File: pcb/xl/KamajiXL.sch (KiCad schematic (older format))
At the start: 31 parts

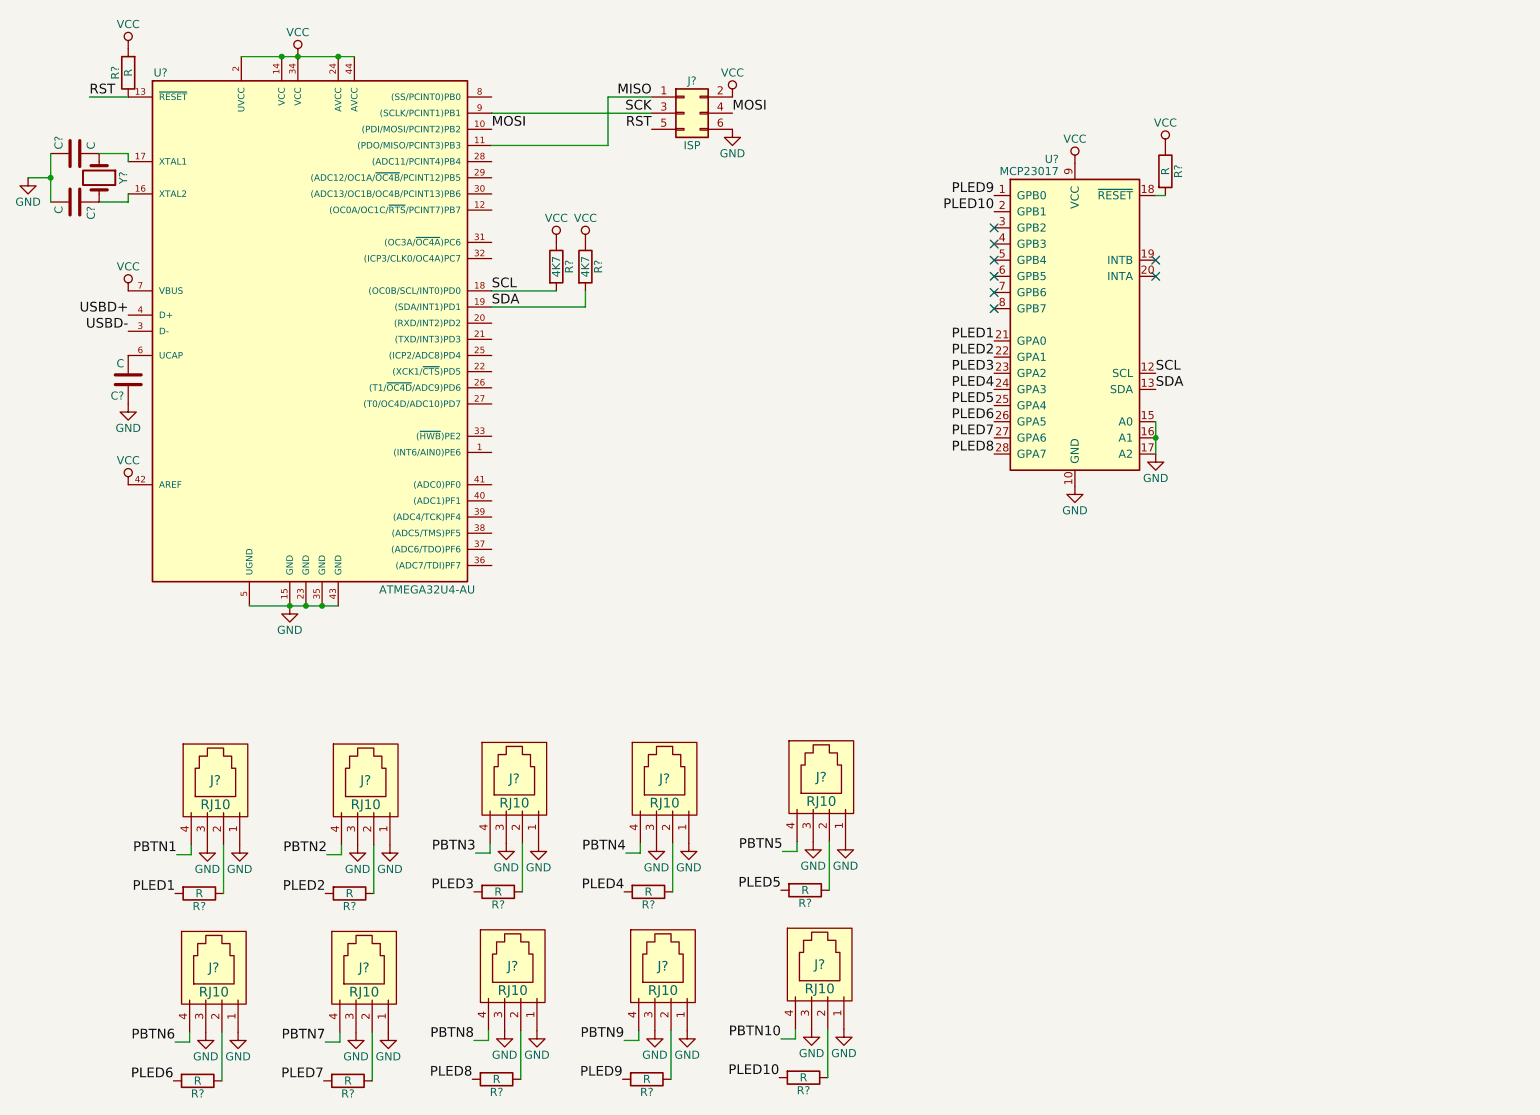
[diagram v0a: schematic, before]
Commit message: put together a minimal schematic for kamaji xl to get an idea about its size
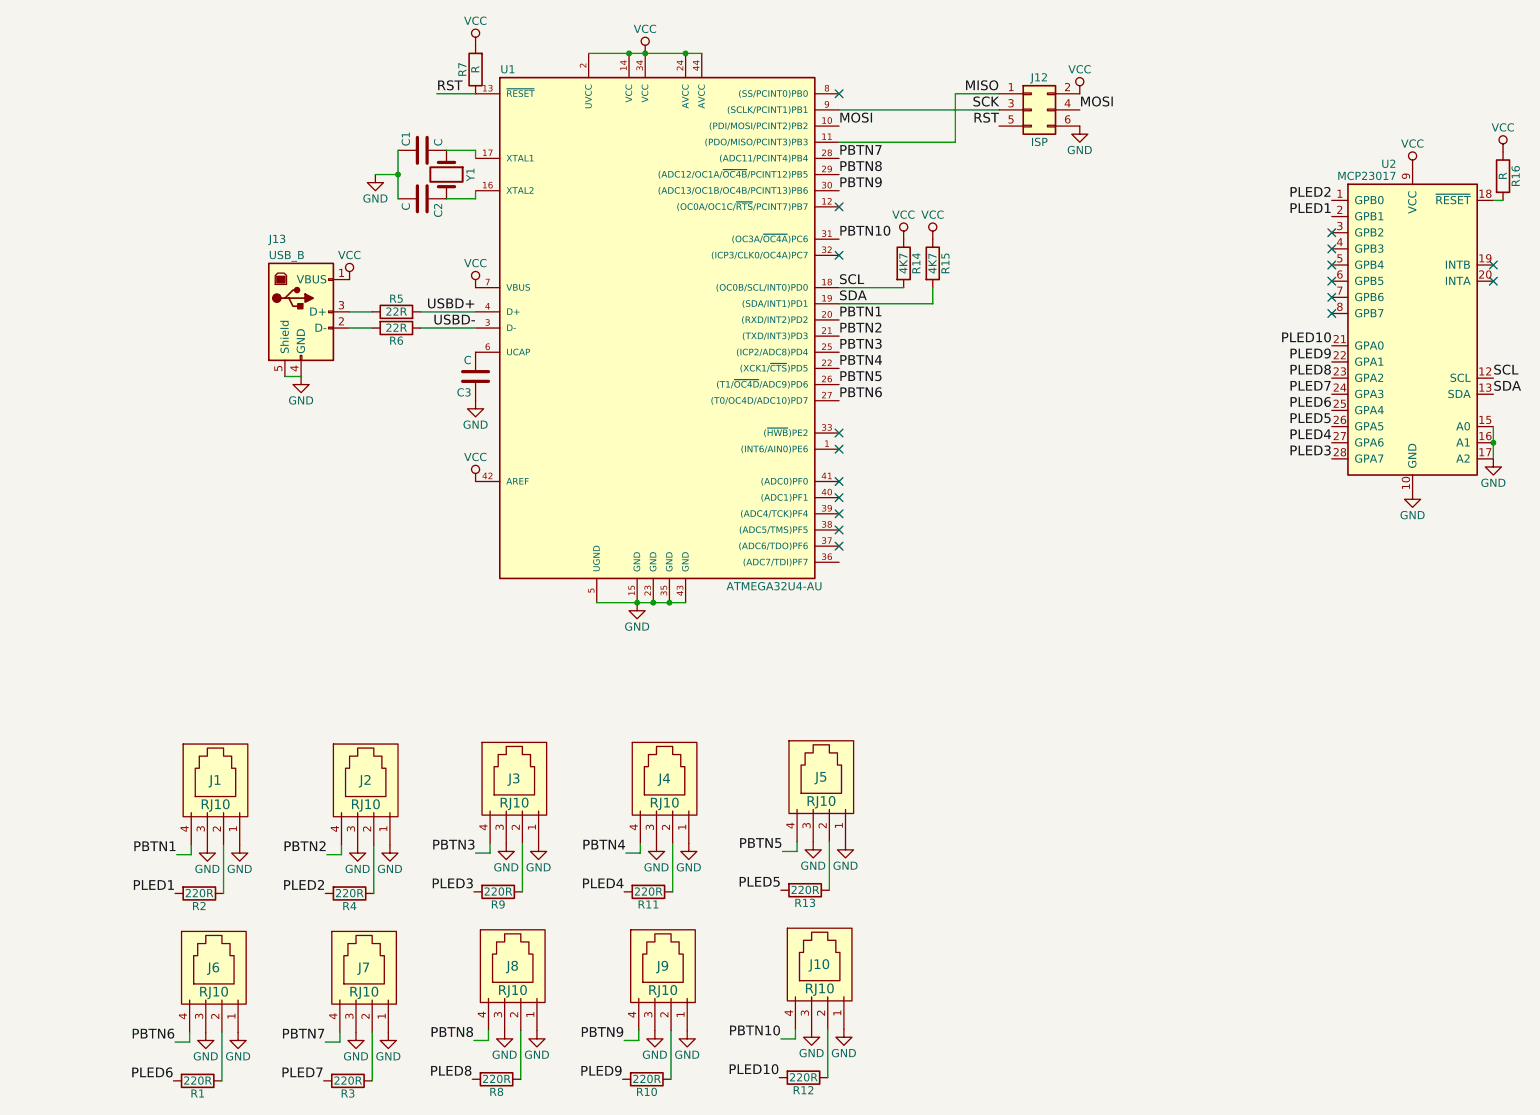
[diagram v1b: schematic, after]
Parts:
- added J13: USB_B, Connectors:USB_B, symbol USB_B
- added R5, R6: 22R, Resistors_SMD:R_1206_HandSoldering, symbol R
- C1, C2, C3: renamed from C?; footprint (none) -> Capacitors_SMD:C_1206_HandSoldering
- J1, J10, J2, J3, J4, J5, J6, J7, J8, J9: renamed from J?; footprint (none) -> kamaji:RJ10
- J12: renamed from J?; footprint (none) -> kamaji:ATmega_ISP_6pin
- R1, R10, R11, R12, R13, R2, R3, R4, R8, R9: renamed from R?; value R -> 220R; footprint (none) -> Resistors_SMD:R_1206_HandSoldering
- R14, R15, R16, R7: renamed from R?; footprint (none) -> Resistors_SMD:R_1206_HandSoldering
- U1: renamed from U?; footprint TQFP44 -> Housings_QFP:TQFP-44_10x10mm_Pitch0.8mm
- U2: renamed from U?; footprint (none) -> Housings_SOIC:SOIC-28W_7.5x17.9mm_Pitch1.27mm
- Y1: renamed from Y?; footprint (none) -> Crystals:Crystal_SMD_HC49-SD_HandSoldering
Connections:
- net GND: now also J13.4 (GND), J13.5 (Shield)
- net PBTN1: now also U1.20 ((RXD/INT2)PD2)
- net PBTN10: now also U1.31 ((OC3A/~OC4A~)PC6)
- net PBTN2: now also U1.21 ((TXD/INT3)PD3)
- net PBTN3: now also U1.25 ((ICP2/ADC8)PD4)
- net PBTN4: now also U1.22 ((XCK1/~CTS~)PD5)
- net PBTN5: now also U1.26 ((T1/~OC4D~/ADC9)PD6)
- net PBTN6: now also U1.27 ((T0/OC4D/ADC10)PD7)
- net PBTN7: now also U1.28 ((ADC11/PCINT4)PB4)
- net PBTN8: now also U1.29 ((ADC12/OC1A/~OC4B~/PCINT12)PB5)
- net PBTN9: now also U1.30 ((ADC13/OC1B/OC4B/PCINT13)PB6)
- net PLED1: now also U2.2 (GPB1); no longer U2.21 (GPA0)
- net PLED10: now also U2.21 (GPA0); no longer U2.2 (GPB1)
- net PLED2: now also U2.1 (GPB0); no longer U2.22 (GPA1)
- net PLED3: now also U2.28 (GPA7); no longer U2.23 (GPA2)
- net PLED4: now also U2.27 (GPA6); no longer U2.24 (GPA3)
- net PLED5: now also U2.26 (GPA5); no longer U2.25 (GPA4)
- net PLED6: now also U2.25 (GPA4); no longer U2.26 (GPA5)
- net PLED7: now also U2.24 (GPA3); no longer U2.27 (GPA6)
- net PLED8: now also U2.23 (GPA2); no longer U2.28 (GPA7)
- net PLED9: now also U2.22 (GPA1); no longer U2.1 (GPB0)
- net USBD+: now also R5.2
- net USBD-: now also R6.1
- net VCC: now also J13.1 (VBUS)
- new net: J13.2 (D-), R6.2
- new net: J13.3 (D+), R5.1
- no-connect marks 8 -> 18
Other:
- moved on the sheet: C1, C2, C3, J12, R14, R15, R16, R7, U1, U2, Y1
